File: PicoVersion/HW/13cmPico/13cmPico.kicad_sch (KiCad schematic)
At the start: 34 parts

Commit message: working version
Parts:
- removed C (x6): C, symbol Device:C
- removed C (x2): C_Polarized_Small, symbol Device:C_Polarized_Small
- removed R (x8): R, symbol Device:R
- removed U: RP2040, RP2040_minimal:RP2040-QFN-56, symbol MCU_RaspberryPi_and_Boards:RP2040
- removed U (x2): LM4562, symbol Amplifier_Operational:LM4562
- removed U: AD8132ARMZ, SOP65P490X110-8N, symbol AD8132ARMZ:AD8132ARMZ
- removed U: CR2013-MI2120, Display:CR2013-MI2120, symbol Driver_Display:CR2013-MI2120
- added C (x9): C, symbol Device:C
- added C: C_Polarized_Small, symbol Device:C_Polarized_Small
- added L: ETC1-1-13TR, ETC1-1-13TR:SM22, symbol ETC1-1-13TR:ETC1-1-13TR
- added R (x6): R, symbol Device:R
- added SW: SW_Push, symbol Switch:SW_Push
- added U (x2): LM4562, symbol Amplifier_Operational:LM4562
- added U: Pico, RPi_Pico:RPi_Pico_SMD_TH, symbol MCU_RaspberryPi_and_Boards:Pico
- added U: AD8346, symbol n3b_tx:AD8346
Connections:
- net +5V: now also R.2
- net GND: now also SW.C, C.1, C.1, C.1, C.1, C.1, C.1, C.1, C.2, L.4, R.1, SW.2, U.10 (COM3), U.13 (COM4), U.14 (COM4), U.3 (COM1), U.4 (COM1), U.9 (COM2)
- net I_out+: now also U.2 (-), U.1 (IBBP)
- net I_out-: now also R.2, U.1, U.2 (IBBN)
- net I_proc: now also R.1, U.26 (GPIO20)
- net Q_out+: now also R.1, U.1, U.16 (QBBP), U.2 (-)
- net Q_out-: now also R.2, U.1, U.15 (QBBP)
- net Q_proc: now also R.1, U.25 (GPIO19)
- net at SW.A: now also U.7 (GPIO5)
- net at SW.B: now also U.6 (GPIO4)
- net IQ_ref renamed IQ_ref2
- net IQ_ref2: now also U.3 (+); no longer U.3 (+), U.3 (+)
- new net: C.2, R.2, U.3 (+) (x2)
- new net: R.1, R.2, U.2 (-)
- new net: SW.1, U.30 (RUN)
- new net: C.1, L.1
- new net: C.2, U.5 (LOIN)
- new net: C.1, L.3
- new net: C.2, U.6 (LOIP)
- new net +3V3: C.2, C.2, C.2, C.2, U.12 (VPS2), U.7 (VPS1), U.8 (ENBL)
- new net IQ_ref1: C.1, C.2, R.1, R.2, U.3 (+)
- new net LO_IN: L.5
- new net RF_Out: U.11 (VOUT)
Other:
- note added: "ADF4351 modulu ya da devresi yer alacak.. internette hazir jkicad projeleri de var"
- note added: "Burdan RF_Out cikip bir 100PF ile SBPF8139 veya benzeri bir on yukseltece gidecek"
- note added: "NOT 2: I- I+ Q- ve Q+ sinyalleri PICO tarafindan gelen 0-3V genlikli sinus sinyaline karsi DC merkezi 1V2 de olan +-0.5 (1Vp-to-p) bir sinyal olmalidir"
- note added: "NOT: I- ile I+ arasindaki gerilim farki 2V olmali... ayni sekilde Q- ve Q+ da"
- title: (none) -> N3B tx
- moved on the sheet: C, R, SW, UA

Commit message: updating TX portion
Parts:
- added C1, C2: 68n, Capacitor_SMD:C_0805_2012Metric, symbol Device:C
- C101, C110, C111, C112: renamed from C; value C -> 47n; footprint (none) -> Capacitor_SMD:C_0805_2012Metric
- C102, C109: renamed from C; value C_Polarized_Small -> 10u; footprint (none) -> Capacitor_SMD:CP_Elec_5x3
- C103, C104: renamed from C; value C -> 4n7; footprint (none) -> Capacitor_SMD:C_0805_2012Metric
- C105, C107, C108, C114: renamed from C; value C -> 100p; footprint (none) -> Capacitor_SMD:C_0805_2012Metric
- C106, C113: renamed from C; value C -> 0.01u; footprint (none) -> Capacitor_SMD:C_0805_2012Metric
- R101, R112: renamed from R; value R -> 5K6; footprint (none) -> Resistor_SMD:R_0805_2012Metric
- R102, R111: renamed from R; value R -> 1K8; footprint (none) -> Resistor_SMD:R_0805_2012Metric
- R103, R104, R106, R107, R109, R110: renamed from R; value R -> 10K; footprint (none) -> Resistor_SMD:R_0805_2012Metric
- SW102: renamed from SW; value SW_Push -> RESET
- renumbered L to L101, SW to SW101, U to U101, U to U102, U to U103, U to U104, U to U105
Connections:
- net +5V: now also U102.8 (V+), U103.8 (V+)
- net GND: now also SW101.S2, U101.13 (GND), U101.18 (GND), U101.23 (GND), U101.28 (GND), U101.3 (GND), U101.33 (AGND), U101.38 (GND), U101.8 (GND), U102.4 (V-), U103.4 (V-), C1.1, C2.1
- net IQ_ref1: now also U103.5 (+); no longer U103.3 (+)
- net IQ_ref2: now also U105.5 (+); no longer U105.3 (+)
- net I_out-: now also U103.7; no longer U103.1
- net I_proc: no longer U101.26 (GPIO20)
- net Q_out-: now also U105.7; no longer U105.1
- net Q_proc: no longer U101.25 (GPIO19)
- net at R106.2, R107.1: now also U105.6 (-); no longer U105.2 (-)
- net at R109.2, R110.1: now also U103.6 (-); no longer U103.2 (-)
- net at U101.6 (GPIO4): no longer SW101.B
- net at U101.7 (GPIO5): no longer SW101.A
- net ROT_TX: now reaches U101.9 (GPIO6)
- net ROT_TX: now also SW101.S1
- new net: C2.2, SW101.A
- new net: C1.2, SW101.B
- new net I_TX: U101.26 (GPIO20)
- new net Q_TX: U101.25 (GPIO19)
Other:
- note added: "ADF4351 modulu ya da devresi yer alacak.."
- note added: "IQ LEVEL SHIFTER"
- note added: "IQ MODULATOR"
- note added: "TX ROTARY"
- note removed: "ADF4351 modulu ya da devresi yer alacak.. internette hazir jkicad projeleri de var"
- moved on the sheet: C101, C102, C103, C104, C105, C106, C107, C108, C109, C110, C111, C112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

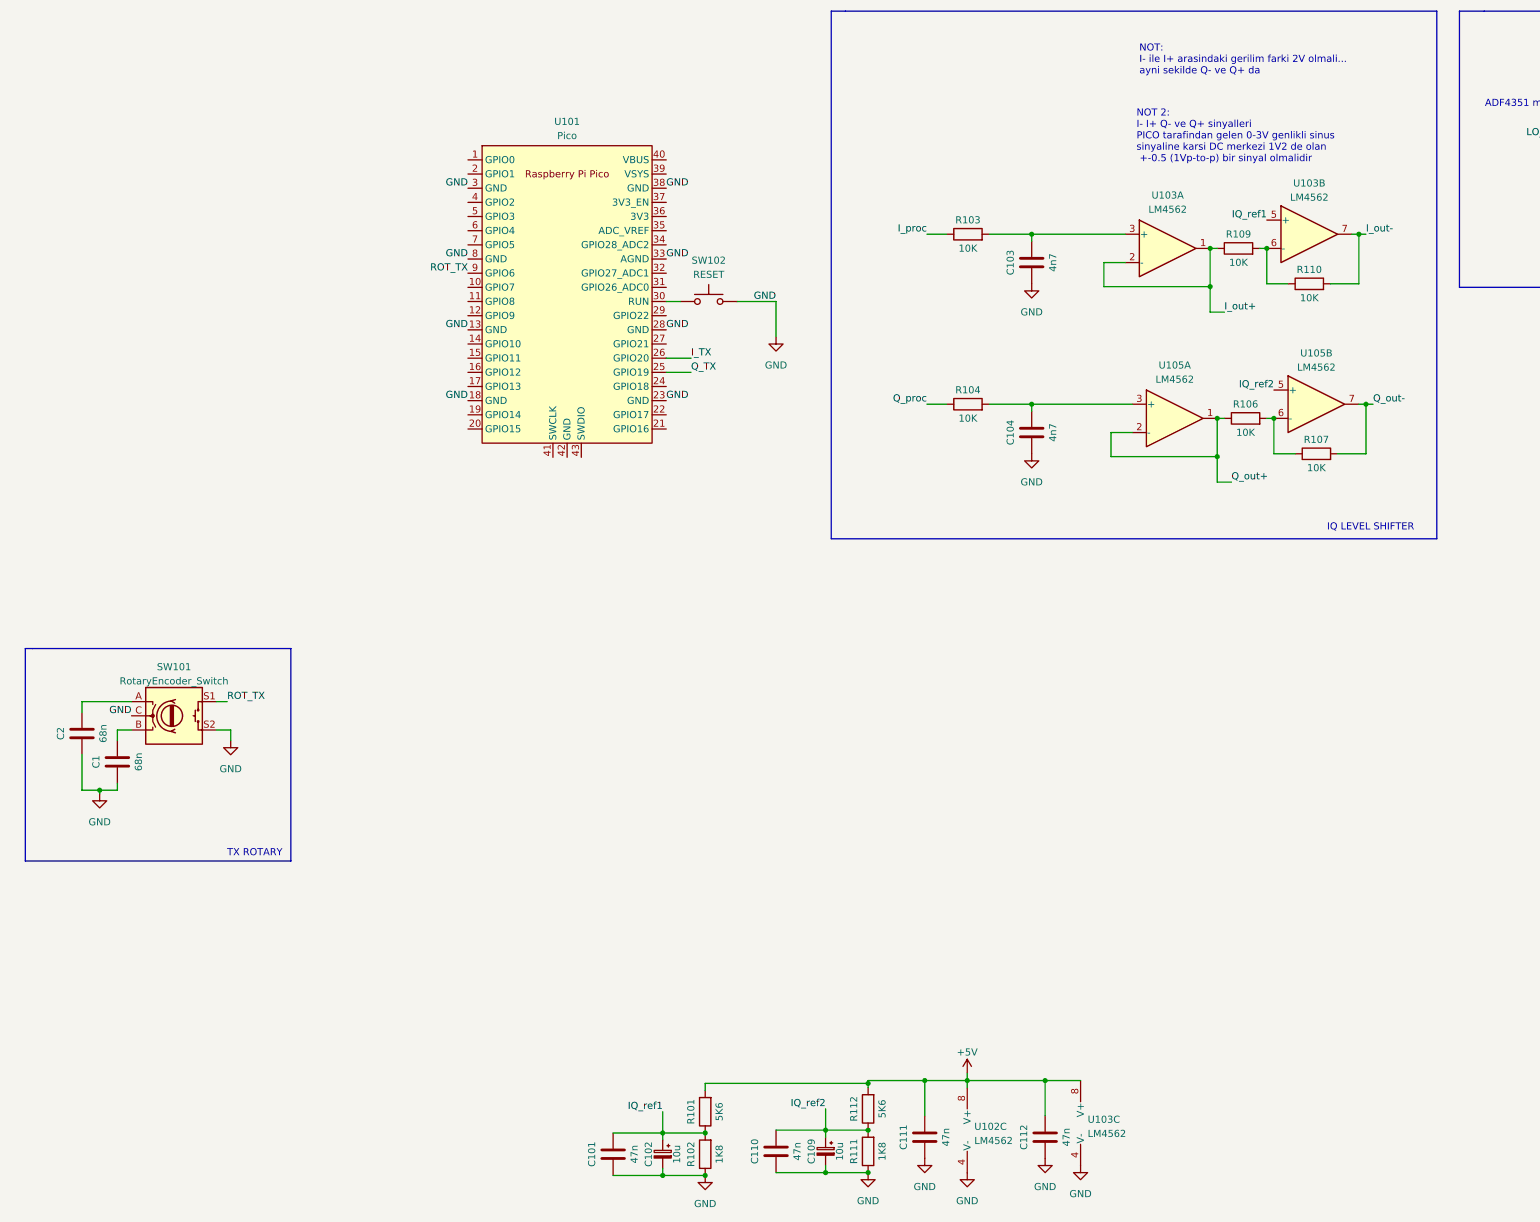
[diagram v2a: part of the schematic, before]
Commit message: keypad added
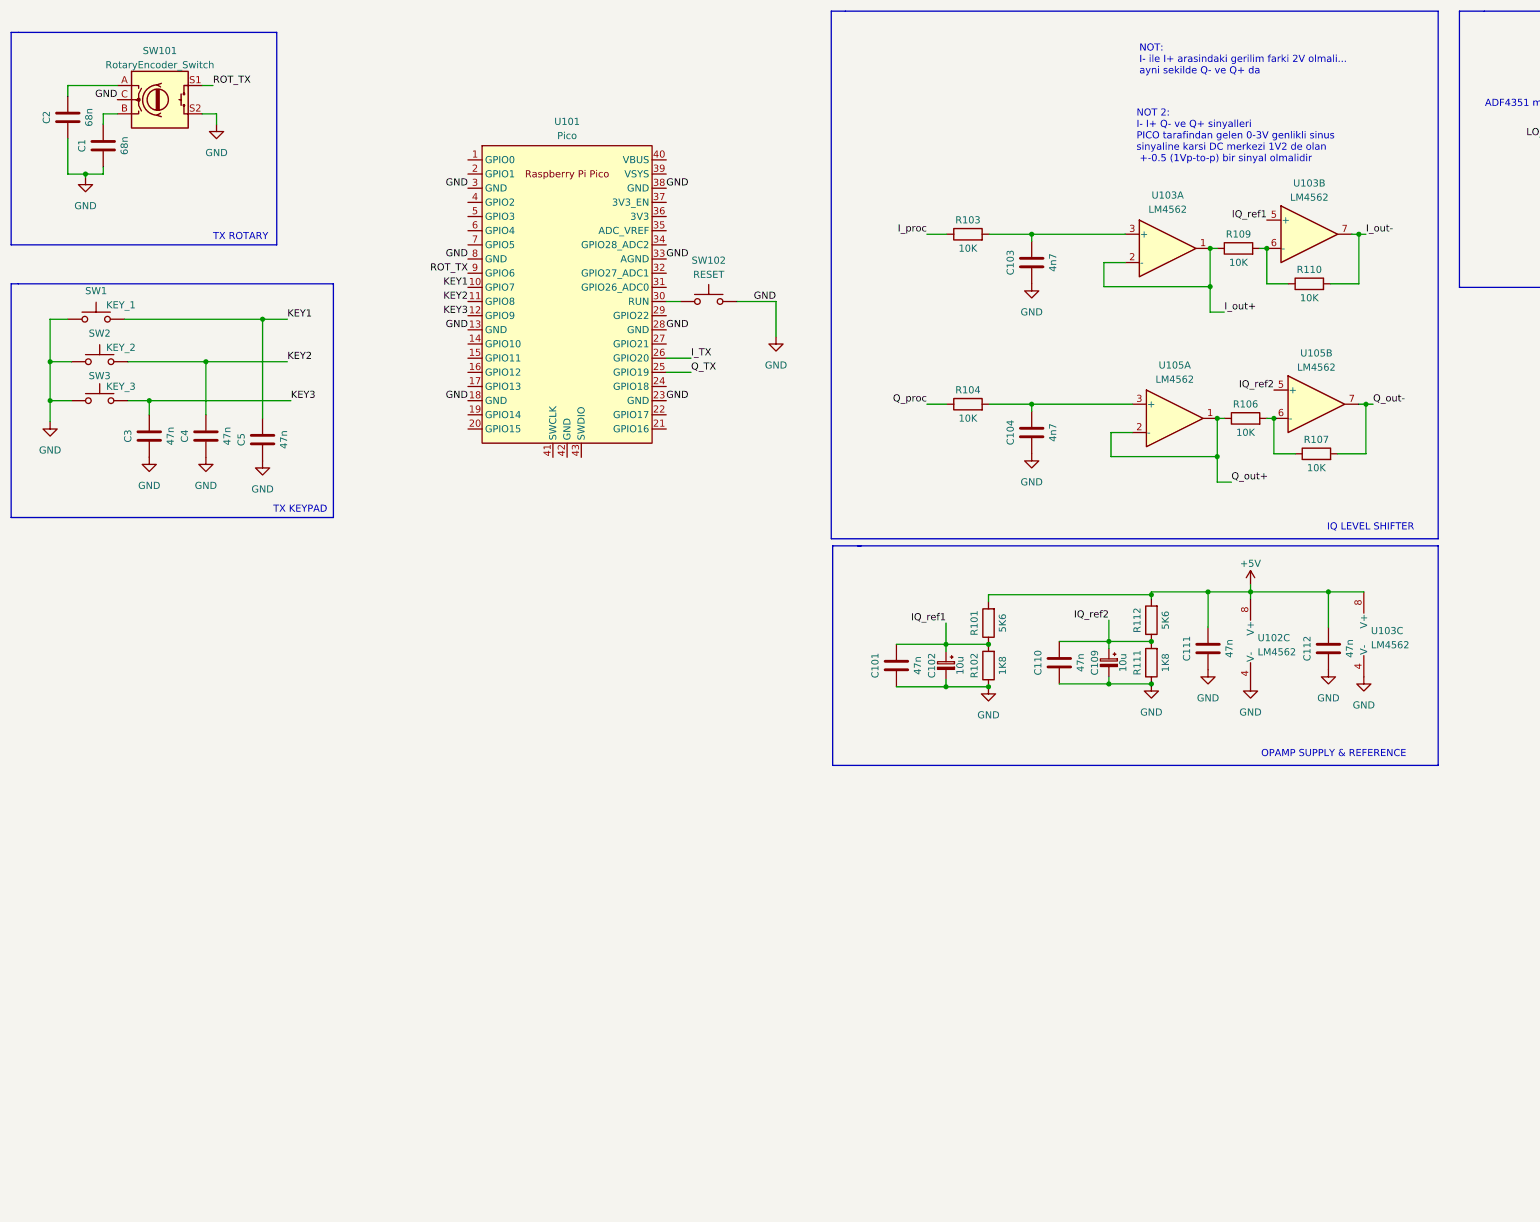
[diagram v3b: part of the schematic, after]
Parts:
- added C3, C4, C5: 47n, Capacitor_SMD:C_0805_2012Metric, symbol Device:C
- added SW1: KEY_1, symbol Switch:SW_Push
- added SW2: KEY_2, symbol Switch:SW_Push
- added SW3: KEY_3, symbol Switch:SW_Push
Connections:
- net GND: now also C3.1, C4.1, C5.1, SW1.1, SW2.1, SW3.1
- net KEY1: now reaches U101.10 (GPIO7)
- net KEY1: now also C5.2, SW1.2
- net KEY2: now reaches U101.11 (GPIO8)
- net KEY2: now also C4.2, SW2.2
- net KEY3: now reaches U101.12 (GPIO9)
- net KEY3: now also C3.2, SW3.2
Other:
- note added: "OPAMP SUPPLY & REFERENCE"
- note added: "TX KEYPAD"
- moved on the sheet: C1, C101, C102, C109, C110, C111, C112, C2, R101, R102, R111, R112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

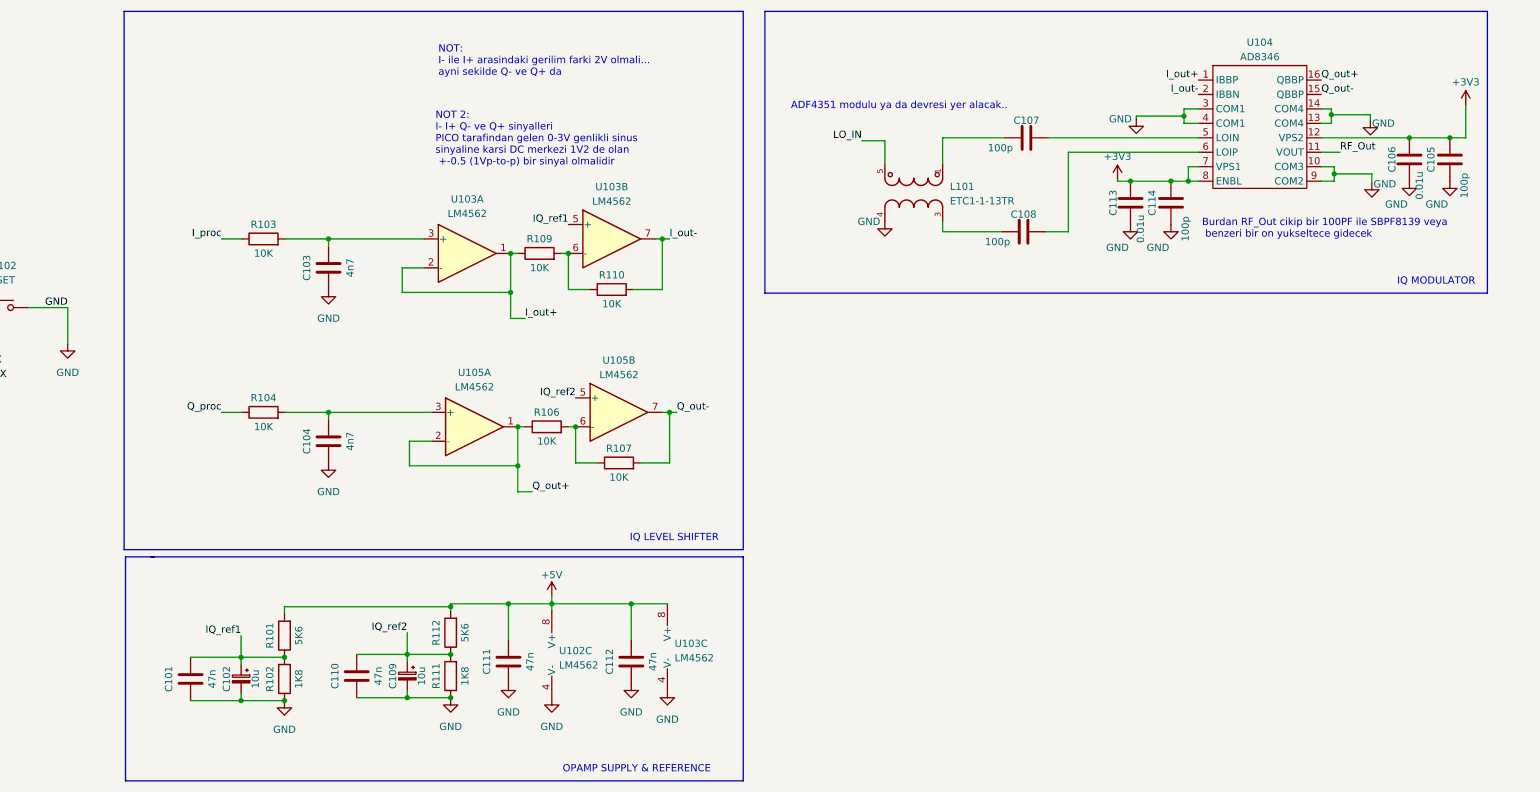
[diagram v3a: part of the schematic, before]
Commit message: ADF4351 Local oscillator added
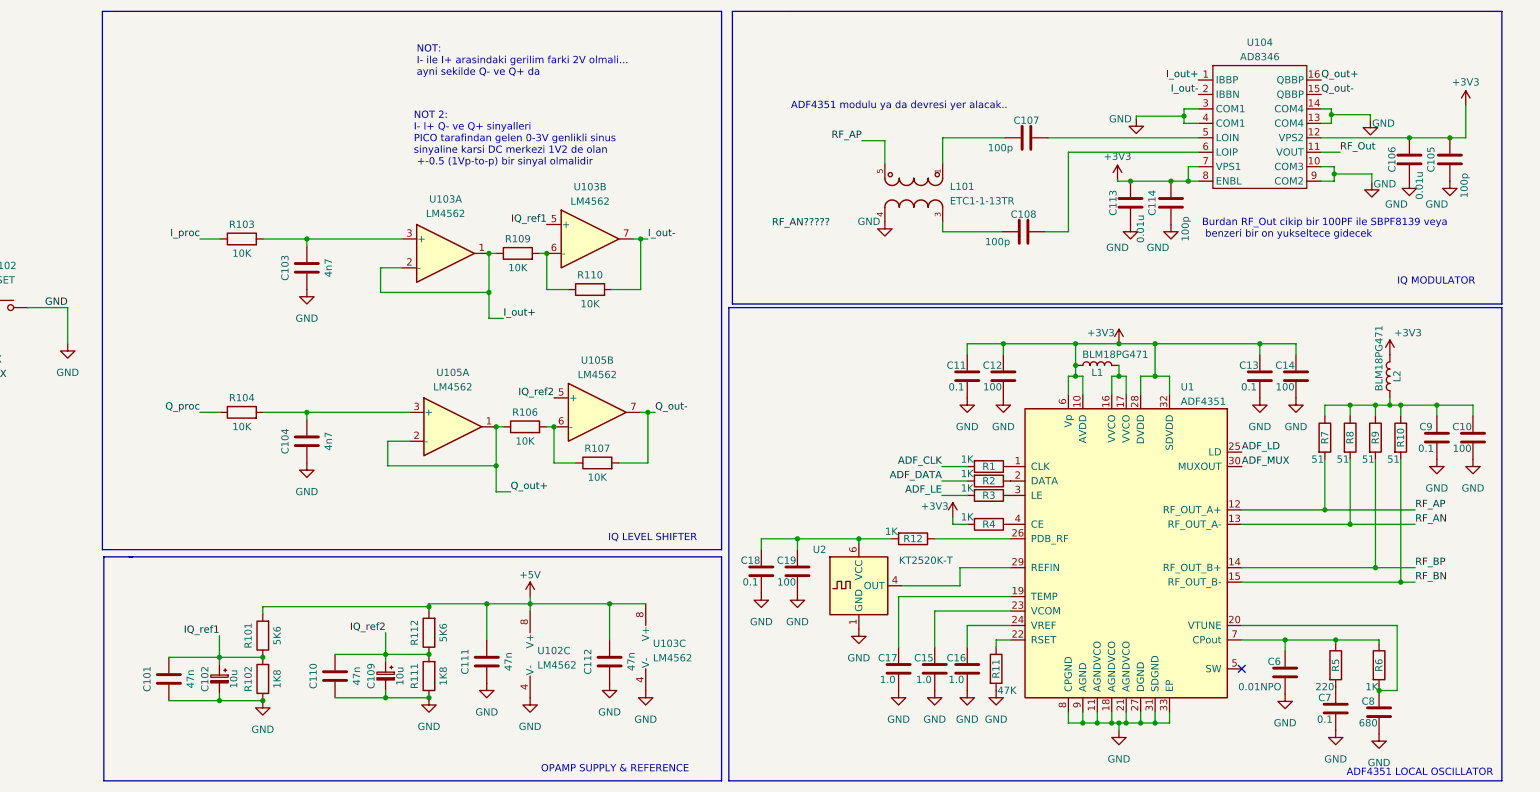
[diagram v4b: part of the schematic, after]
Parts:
- added C10, C12, C14, C19: 100, Capacitor_SMD:C_0805_2012Metric, symbol Device:C
- added C11, C13, C18, C7, C9: 0.1, Capacitor_SMD:C_0805_2012Metric, symbol Device:C
- added C15, C16, C17: 1.0, Capacitor_SMD:C_0805_2012Metric, symbol Device:C
- added C6: 0.01NPO, Capacitor_SMD:C_0805_2012Metric, symbol Device:C
- added C8: 680, Capacitor_SMD:C_0805_2012Metric, symbol Device:C
- added L1, L2: BLM18PG471, symbol Device:L
- added R1, R12, R2, R3, R4, R6: 1K, Resistor_SMD:R_0805_2012Metric, symbol Device:R
- added R10, R7, R8, R9: 51, Resistor_SMD:R_0805_2012Metric, symbol Device:R
- added R11: 47K, Resistor_SMD:R_0805_2012Metric, symbol Device:R
- added R5: 220, Resistor_SMD:R_0805_2012Metric, symbol Device:R
- added U1: ADF4351, Package_CSP:LFCSP-32-1EP_5x5mm_P0.5mm_EP3.25x3.25mm, symbol Timer_PLL:ADF4351
- added U2: KT2520K-T, Oscillator:Oscillator_SMD_Kyocera_2520-6Pin_2.5x2.0mm, symbol Oscillator:KT2520K-T
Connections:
- net +3V3: now also C11.2, C12.2, C13.2, C14.2, L1.1, L2.2, R4.2, U1.10 (AVDD), U1.28 (DVDD), U1.32 (SDVDD), U1.6 (Vp)
- net GND: now also C10.1, C11.1, C12.1, C13.1, C14.1, C15.1, C16.1, C17.1, C18.1, C19.1, C6.1, C7.1, C8.1, C9.1, R11.2, U1.11 (AGNDVCO), U1.18 (AGNDVCO), U1.21 (AGNDVCO), U1.27 (DGND), U1.31 (SDGND), U1.33 (EP), U1.8 (CPGND), U1.9 (AGND), U2.1 (GND), U2.3 (GND)
- net LO_IN renamed RF_AP
- net RF_AP: now also R7.2, U1.12 (RF_OUT_A+)
- new net: R1.1, U1.1 (CLK)
- new net: L1.2, U1.16 (VVCO), U1.17 (VVCO)
- new net: C17.2, U1.19 (TEMP)
- new net: R2.1, U1.2 (DATA)
- new net: C8.2, R6.2, U1.20 (VTUNE)
- new net: R11.1, U1.22 (RSET)
- new net: C15.2, U1.23 (VCOM)
- new net: C16.2, U1.24 (VREF)
- new net: R12.1, U1.26 (PDB_RF)
- new net: U1.29 (REFIN), U2.4 (OUT)
- new net: R3.1, U1.3 (LE)
- new net: R4.1, U1.4 (CE)
- new net: C6.2, R5.1, R6.1, U1.7 (CPout)
- new net: C10.2, C9.2, L2.1, R10.1, R7.1, R8.1, R9.1
- new net: C18.2, C19.2, R12.2, U2.6 (VCC)
- new net: C7.2, R5.2
- new net ADF_CLK: R1.2
- new net ADF_DATA: R2.2
- new net ADF_LD: U1.25 (LD)
- new net ADF_LE: R3.2
- new net ADF_MUX: U1.30 (MUXOUT)
- new net RF_AN: R8.2, U1.13 (RF_OUT_A-)
- new net RF_BN: R10.2, U1.15 (RF_OUT_B-)
- new net RF_BP: R9.2, U1.14 (RF_OUT_B+)
- no-connect marks 0 -> 1
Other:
- note added: "ADF4351 LOCAL OSCILLATOR"
- title: N3B tx -> N3B TX
- moved on the sheet: C101, C102, C103, C104, C109, C110, C111, C112, R101, R102, R103, R104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
